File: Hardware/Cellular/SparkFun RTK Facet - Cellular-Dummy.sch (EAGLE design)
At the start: 64 parts, among them IC1 SN74AVC4T774PW, J1 FPC_12_0.5MM_BACKFLIP, J18 SARA_USB, J2 NANO_SIM, J3 U.FL, J6 DIAG, Q2 310mA/60V/1.6Ω, Q3 310mA/60V/1.6Ω, Q4 310mA/60V/1.6Ω, Q5 20V/0.2A/8MHz/1.2Ω/1Vth, Q7 310mA/60V/1.6Ω, U1 SARA-R510M8S, U8 74HC1G04

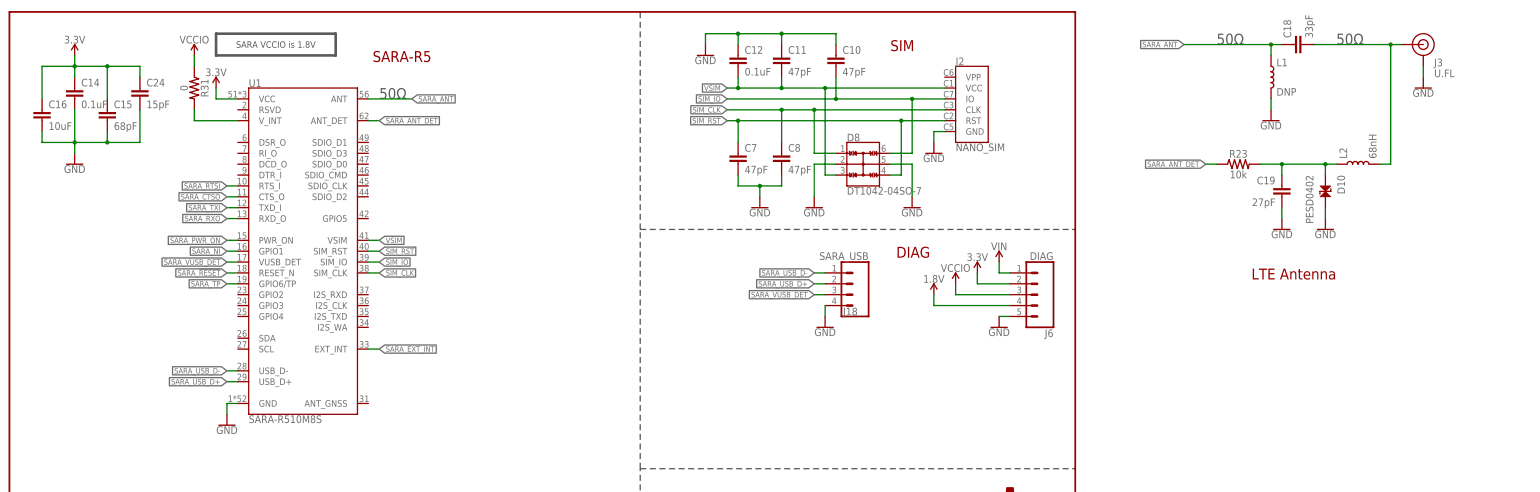
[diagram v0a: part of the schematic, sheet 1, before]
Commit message: Double up 3.3V on cell connector. Create dummy test board.
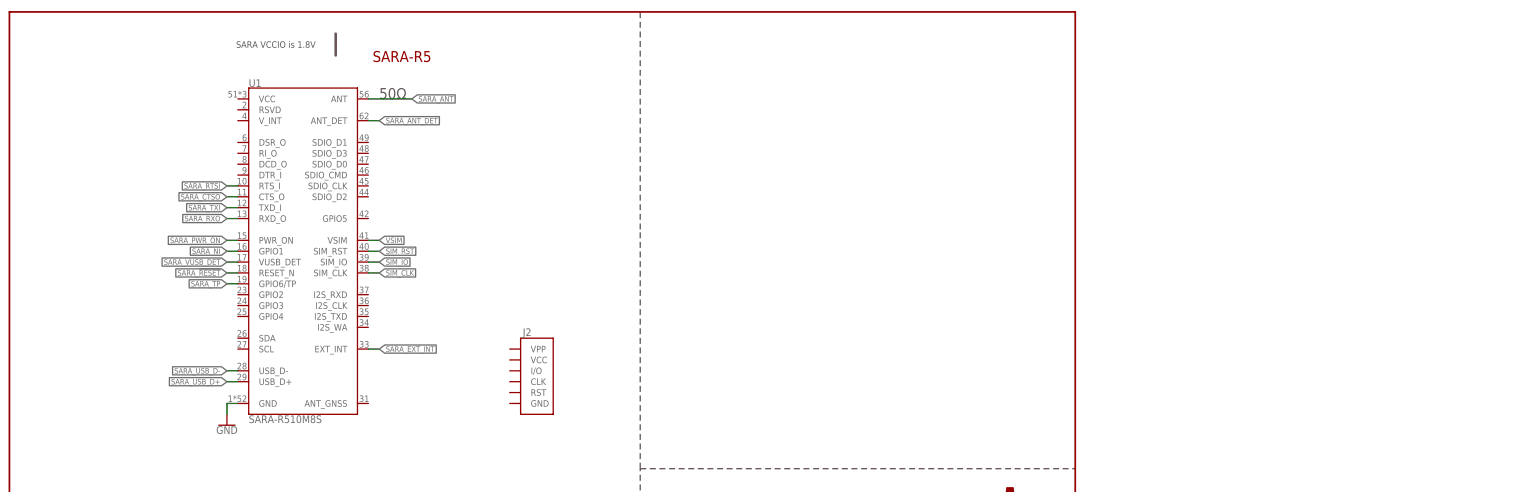
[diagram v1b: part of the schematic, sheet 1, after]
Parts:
- removed C10, C11, C7, C8: 47pF, SparkFun-Capacitors:47PF-0603-50V-5%
- removed C12, C14: 0.1uF, SparkFun-Capacitors:0.1UF-0603-25V-5%
- removed C15: 68pF, SparkFun-Capacitors:68PF-0603-50V-5%
- removed C16: 10uF, SparkFun-Capacitors:10UF-0603-6.3V-20%
- removed C18: 33pF, New_Parts:33PF-0402-25V-5%-X7R
- removed C19: 27pF, New_Parts:27PF-0402-25V-5%-X7R
- removed C22: 0.1uF, SparkFun-Capacitors:0.1UF-0603-25V-(+80/-20%)
- removed C24: 15pF, SparkFun-Capacitors:15PF-0603-50V-5%
- removed D10: PESD0402, New_Parts:PESD0402
- removed D13: BLUE, SparkFun-LED:LED-BLUE0603
- removed D14: WHITE, SparkFun-LED:LED-WHITE0603
- removed D8: DT1042-04SO-7, ublox:TVS_DIODE_ARRAY_4DT1042-04SO-7
- removed FRAME2: FRAME-LETTERNO_PACKAGE, SparkFun-Aesthetics:FRAME-LETTERNO_PACKAGE
- removed IC1: SN74AVC4T774PW, New_Parts:SN74AVC4T774PW
- removed J18: SARA_USB, SparkFun-Connectors:CONN_041X04_NO_SILK
- removed J3: U.FL, SparkFun-Connectors:U.FL2PIN
- removed J6: DIAG, SparkFun-Connectors:CONN_05NO_SILK
- removed JP19: JUMPER-SMT_3_1-NC_TRACE_SILK, SparkFun-Jumpers:JUMPER-SMT_3_1-NC_TRACE_SILK
- removed L1: DNP, New_Parts:INDUCTOR_DNP-0402
- removed L2: 68nH, New_Parts:68NH-0402
- removed Q2, Q3, Q4, Q7: 310mA/60V/1.6Ω, SparkFun-DiscreteSemi:MOSFET-NCH-2N7002PW
- removed Q5: 20V/0.2A/8MHz/1.2Ω/1Vth, SparkFun-DiscreteSemi:MOSFET-NCH-RE1C00UNTL
- removed R18, R19, R39, R44: 100k, SparkFun-Resistors:100KOHM-0603-1/10W-1%
- removed R23: 10k, SparkFun-Resistors:10KOHM-0603-1/10W-1%
- removed R27, R28, R34, R42, R43: 1k, SparkFun-Resistors:1KOHM-0603-1/10W-1%
- removed R29, R30: 2.2k, SparkFun-Resistors:2.2KOHM-0603-1/10W-1%
- removed R31: 0, SparkFun-Resistors:0OHM-0603-1/10W
- removed R35: 470, SparkFun-Resistors:470OHM-0603-1/10W-1%
- removed TP1, TP12, TP13, TP2, TP3, TP4, TP5, TP6, TP7, TP8: TEST-POINT3, SparkFun-Connectors:TEST-POINT3
- removed U8: 74HC1G04, SparkFun-IC-Logic:74HC1G04
- J2: value NANO_SIM -> (none); device ublox:NANO_SIMWURTH -> SparkFun-Connectors:SIMHOLDERNANOSIM
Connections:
- removed net 1.8V: J6.4
- removed net LTE_NI: Q3.D, R35.1, R39.1
- removed net N$15: C18.2, J3.SIGNAL, L2.2
- removed net N$16: C19.1, D10.1, L2.1, R23.2
- removed net N$26: Q2.G, R27.2
- removed net N$27: Q4.G, R28.2
- removed net N$28: R28.1, U8G1.Y
- removed net N$31: R31.2, U1.V_INT
- removed net N$35: Q3.G, R34.2
- removed net N$37: D13.C, R35.2
- removed net N$43: JP19.2, Q5.S, R29.1
- removed net N$47: Q7.G, R42.2
- removed net N$49: D14.C, R43.2
- removed net SARA_!ON!: Q7.D, R43.1, R44.1, TP13.1
- removed net SARA_GPIO3: JP19.1
- removed net VCCIO: C22.1, IC1.DIR1, IC1.DIR3, IC1.VCCA, J6.3, Q5.G, R29.2, R31.1, R42.1
- removed net VIN: J6.1
- net 3.3V: no longer C14.1, C15.1, C16.1, C24.1, D13.A, D14.A, IC1.VCCB, J6.2, R30.2, R39.2, R44.2, U1.VCC, U8G2.P$V+
- net GND: no longer C10.1, C11.1, C12.1, C14.2, C15.2, C16.2, C19.2, C22.2, C24.2, C7.2, C8.2, D10.2, D8.2, D8.5, IC1.!OE, IC1.DIR2, IC1.DIR4, IC1.GND, J18.4, J2.GND, J3.GND, J6.5, L1.2, Q2.S, Q3.S, Q4.S, Q7.S, R18.2, R19.1, U8G2.P$V-
- net LTE_!RESET!: no longer U8G1.A
- net LTE_CTSI: no longer IC1.B4, R19.2, TP8.1
- net LTE_INT: no longer Q5.D, R30.1, TP12.1
- net LTE_PWR_ON: no longer R18.1, R27.1
- net LTE_RTSO: no longer IC1.B3, TP7.1
- net LTE_RXI: no longer IC1.B2, TP6.1
- net LTE_TXO: no longer IC1.B1, TP5.1
- net SARA_!RESET!: no longer Q4.D
- net SARA_ANT: no longer C18.1, L1.1
- net SARA_ANT_DET: no longer R23.1
- net SARA_CTSO: no longer IC1.A3, TP3.1
- net SARA_EXT_INT: no longer JP19.3
- net SARA_NI: no longer R34.1
- net SARA_PWR_ON: no longer Q2.D
- net SARA_RTSI: no longer IC1.A4, TP4.1
- net SARA_RXO: no longer IC1.A1, TP1.1
- net SARA_TXI: no longer IC1.A2, TP2.1
- net SARA_USB_D+: no longer J18.2
- net SARA_USB_D-: no longer J18.1
- net SARA_VUSB_DET: no longer J18.3
- net SIM_CLK: no longer C8.1, D8.1, J2.CLK
- net SIM_IO: no longer C10.2, D8.6, J2.IO
- net SIM_RST: no longer C7.1, D8.4, J2.RST
- net VSIM: no longer C11.2, C12.2, D8.3, J2.VCC
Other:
- note removed: "DIAG"
- note removed: "LTE Antenna"
- note removed: "SARA LEDs"
- note removed: "SARA Level Shifting"
- note removed: "SARA-R5 VCC Design Notes:"
- note removed: "SIM"
- note removed: "VCC: Min. 3.3V Typ. 3.8V Max. 4.4V VCC Extended: Min. 3.0V Max. 4.5V Worst case: Maximum current draw during Tx: 395mA Estimated current for other components: 100mA Total maximum current draw: ~500mA AP7361C-33 drop out voltage: ~170mV at: 500mA output current; Vout = 3.3V; 25°C D7 LSM115J Schottky diode forward voltage: ~210mV at: 500mA; 25°C AP7361C 3.3V output will start to fall when the batte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"

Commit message: Change to push push socket on cellular board.
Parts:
- J2: value (none) -> NANO; device SparkFun-Connectors:SIMHOLDERNANOSIM -> SparkFun-Connectors:SIMHOLDER-PUSHPUSH
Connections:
- new net N$1: J2.VCC
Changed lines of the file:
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@@
 <layer number="56" name="wert" color="7" fill="1" visible="no" active="no"/>
 <layer number="57" name="tCAD" color="7" fill="1" visible="no" active="no"/>
+<layer number="58" name="bCAD" color="7" fill="1" visible="no" active="no"/>
 <layer number="59" name="tCarbon" color="7" fill="1" visible="no" active="no"/>
 <layer number="60" name="bCarbon" color="7" fill="1" visible="no" active="no"/>
@@
 <layer number="250" name="Descript" color="7" fill="1" visible="yes" active="yes"/>
 <layer number="251" name="SMDround" color="7" fill="1" visible="yes" active="yes"/>
+<layer number="253" name="Extra" color="7" fill="1" visible="no" active="no"/>
 <layer number="254" name="cooling" color="7" fill="1" visible="yes" active="yes"/>
 <layer number="255" name="routoute" color="7" fill="1" visible="yes" active="yes"/>
@@
 <part name="GND33" library="SparkFun-PowerSymbols" deviceset="GND" device=""/>
 <part name="SUPPLY1" library="SparkFun-PowerSymbols" deviceset="VOUT" device=""/>
-<part name="J2" library="SparkFun-Connectors" deviceset="SIMHOLDER" device="NANOSIM"/>
+<part name="J2" library="SparkFun-Connectors" deviceset="SIMHOLDER" device="-PUSHPUSH" value="NANO"/>
 </parts>
 <sheets>
@@
 </segment>
 </net>
+<net name="N$1" class="0">
+<segment>
+<pinref part="J2" gate="J1" pin="VCC"/>
+<wire x1="116.84" y1="104.14" x2="114.3" y2="104.14" width="0.1524" layer="91"/>
+<label x="114.3" y="104.14" size="1.27" layer="95" rot="R180" xref="yes"/>
+</segment>
+</net>
